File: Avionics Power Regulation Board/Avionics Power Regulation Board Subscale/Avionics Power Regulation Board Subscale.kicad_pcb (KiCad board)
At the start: 2 copper layers, 101.8 x 59.5 mm, 16 parts, among them J1 Conn_01x04_Socket, J2 Conn_01x07_Socket, J3 Conn_01x06_Socket, J4 Conn_01x08_Socket, J5 Conn_01x05_Socket, U1 SC0917

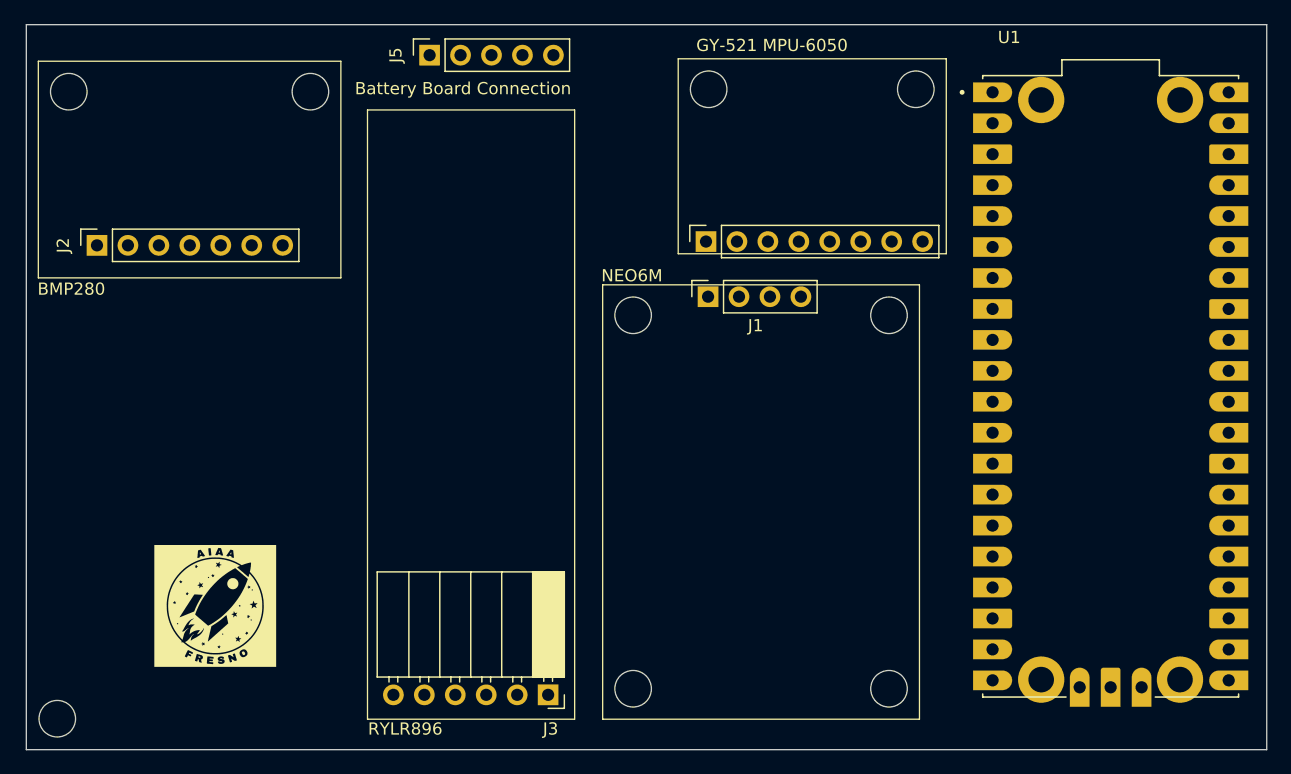
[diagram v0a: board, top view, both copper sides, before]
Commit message: Adding to the Avionics Sensors Board
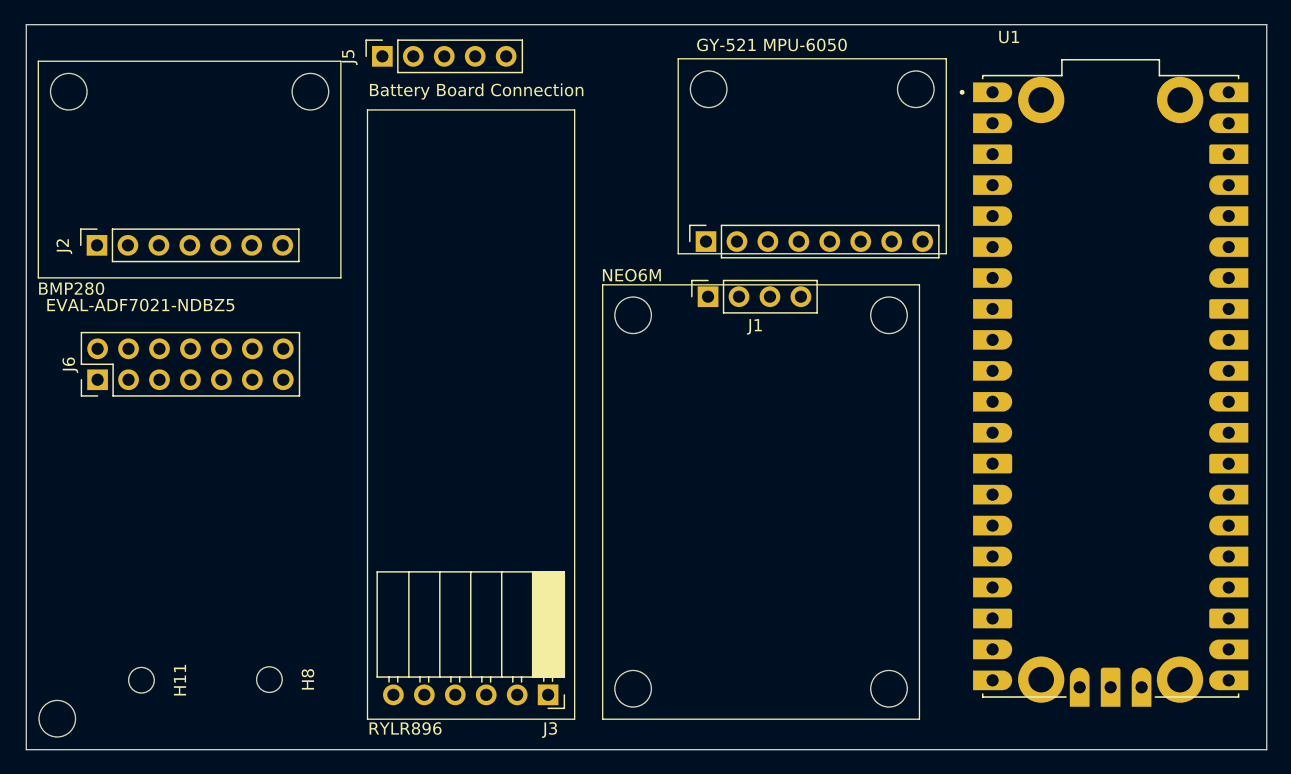
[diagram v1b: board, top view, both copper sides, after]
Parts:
- removed G***: LOGO, AIAA Logo:AIAA Logo
- added H11: MountingHole, MountingHole:MountingHole_2.1mm, F.Cu at (144.4, 92.7)
- added H8: MountingHole, MountingHole:MountingHole_2.1mm, F.Cu at (154.9, 92.7)
- added J6: Conn_02x07_Odd_Even, Connector_PinHeader_2.54mm:PinHeader_2x07_P2.54mm_Vertical, F.Cu at (140.8, 68.0)
- moved J5 3.88 mm to (164.2, 41.5)
